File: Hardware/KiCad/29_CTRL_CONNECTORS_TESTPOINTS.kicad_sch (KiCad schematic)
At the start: 0 parts

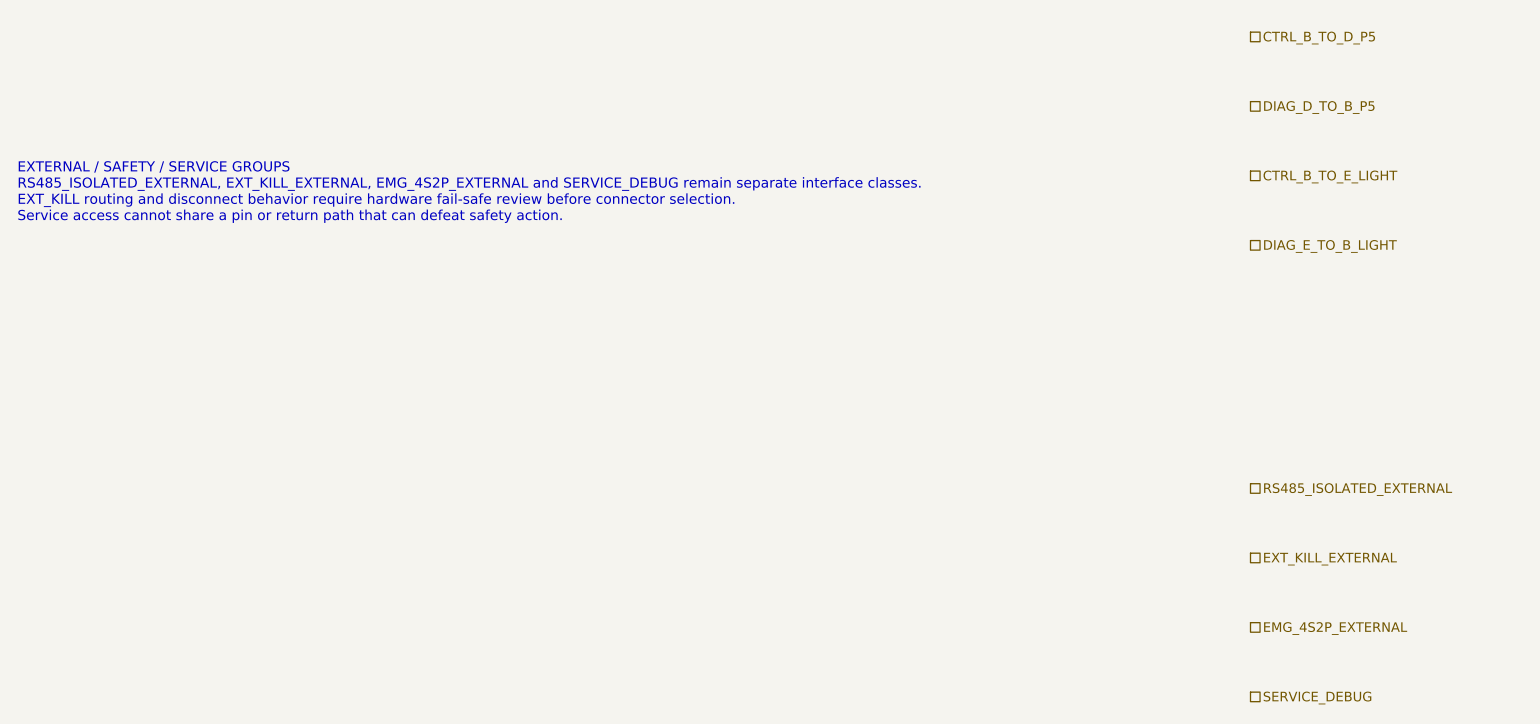
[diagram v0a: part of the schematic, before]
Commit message: hardware: align PCB-B external connector group names
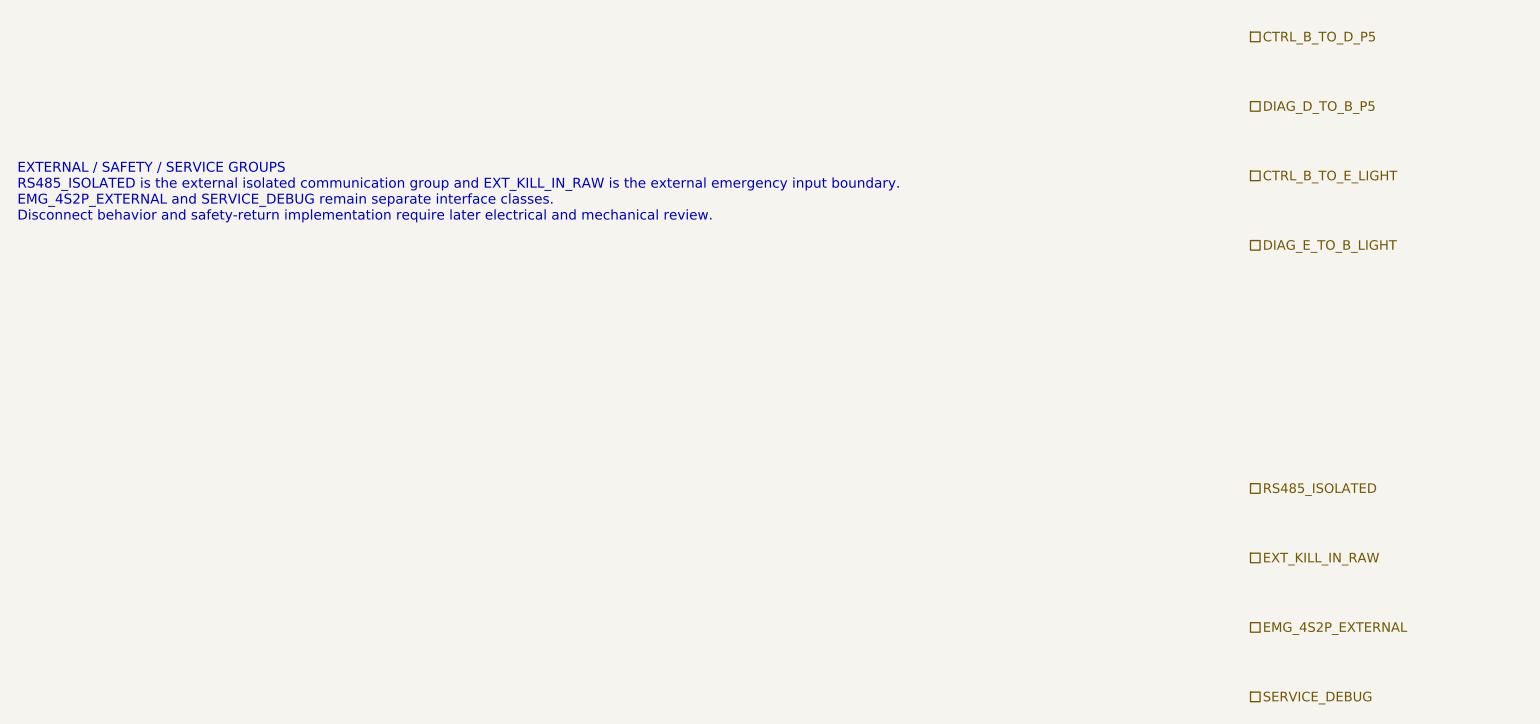
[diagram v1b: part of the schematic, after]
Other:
- note added: "EXTERNAL / SAFETY / SERVICE GROUPS RS485_ISOLATED is the external isolated communication group and EXT_KILL_IN_RAW is the external emergency input boundary. EMG_4S2P_EXTERNAL and SERVICE_DEBUG remain separate interface classes. Disconnect behavior and safety-return implementation require later electrical and mechanical review."
- note removed: "EXTERNAL / SAFETY / SERVICE GROUPS RS485_ISOLATED_EXTERNAL, EXT_KILL_EXTERNAL, EMG_4S2P_EXTERNAL and SERVICE_DEBUG remain separate interface classes. EXT_KILL routing and disconnect behavior require hardware fail-safe review before connector selection. Service access cannot share a pin or return path that can defeat safety action."
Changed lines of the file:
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@@
 		(title "29_CTRL_CONNECTORS_TESTPOINTS - logical connector and test boundary")
 		(date "2026-07-15")
-		(rev "B0")
+		(rev "B1")
 		(company "Gonoboben/plataVM")
-		(comment 1 "Architecture Level A/B: interboard, external, EMG and service interface grouping")
+		(comment 1 "Interface consistency: canonical RS485_ISOLATED and EXT_KILL_IN_RAW groups")
 		(comment 2 "No connector family, pin count, pinout, cable, testpoint technology or footprint selected")
 	)
@@
 		(uuid "ctrl-reserve-00000029-0000-4000-8000-000000000102")
 	)
-	(text "EXTERNAL / SAFETY / SERVICE GROUPS\nRS485_ISOLATED_EXTERNAL, EXT_KILL_EXTERNAL, EMG_4S2P_EXTERNAL and SERVICE_DEBUG remain separate interface classes.\nEXT_KILL routing and disconnect behavior require hardware fail-safe review before connector selection.\nService access cannot share a pin or return path that can defeat safety action."
+	(text "EXTERNAL / SAFETY / SERVICE GROUPS\nRS485_ISOLATED is the external isolated communication group and EXT_KILL_IN_RAW is the external emergency input boundary.\nEMG_4S2P_EXTERNAL and SERVICE_DEBUG remain separate interface classes.\nDisconnect behavior and safety-return implementation require later electrical and mechanical review."
 		(exclude_from_sim no)
 		(at 12 138 0)
-		(effects (font (size 1.16 1.16)) (justify left))
+		(effects (font (size 1.14 1.14)) (justify left))
 		(uuid "ctrl-reserve-00000029-0000-4000-8000-000000000103")
 	)
@@
 	(hierarchical_label "CTRL_B_TO_E_LIGHT" (shape passive) (exclude_from_sim no) (at 154 136 0) (effects (font (size 1.1 1.1)) (justify left)) (uuid "ctrl-reserve-00000029-0000-4000-8000-000000000208"))
 	(hierarchical_label "DIAG_E_TO_B_LIGHT" (shape passive) (exclude_from_sim no) (at 154 144 0) (effects (font (size 1.1 1.1)) (justify left)) (uuid "ctrl-reserve-00000029-0000-4000-8000-000000000209"))
-	(hierarchical_label "RS485_ISOLATED_EXTERNAL" (shape passive) (exclude_from_sim no) (at 154 172 0) (effects (font (size 1.1 1.1)) (justify left)) (uuid "ctrl-reserve-00000029-0000-4000-8000-000000000210"))
-	(hierarchical_label "EXT_KILL_EXTERNAL" (shape passive) (exclude_from_sim no) (at 154 180 0) (effects (font (size 1.1 1.1)) (justify left)) (uuid "ctrl-reserve-00000029-0000-4000-8000-000000000211"))
+	(hierarchical_label "RS485_ISOLATED" (shape passive) (exclude_from_sim no) (at 154 172 0) (effects (font (size 1.1 1.1)) (justify left)) (uuid "ctrl-reserve-00000029-0000-4000-8000-000000000210"))
+	(hierarchical_label "EXT_KILL_IN_RAW" (shape passive) (exclude_from_sim no) (at 154 180 0) (effects (font (size 1.1 1.1)) (justify left)) (uuid "ctrl-reserve-00000029-0000-4000-8000-000000000211"))
 	(hierarchical_label "EMG_4S2P_EXTERNAL" (shape passive) (exclude_from_sim no) (at 154 188 0) (effects (font (size 1.1 1.1)) (justify left)) (uuid "ctrl-reserve-00000029-0000-4000-8000-000000000212"))
 	(hierarchical_label "SERVICE_DEBUG" (shape passive) (exclude_from_sim no) (at 154 196 0) (effects (font (size 1.1 1.1)) (justify left)) (uuid "ctrl-reserve-00000029-0000-4000-8000-000000000213"))

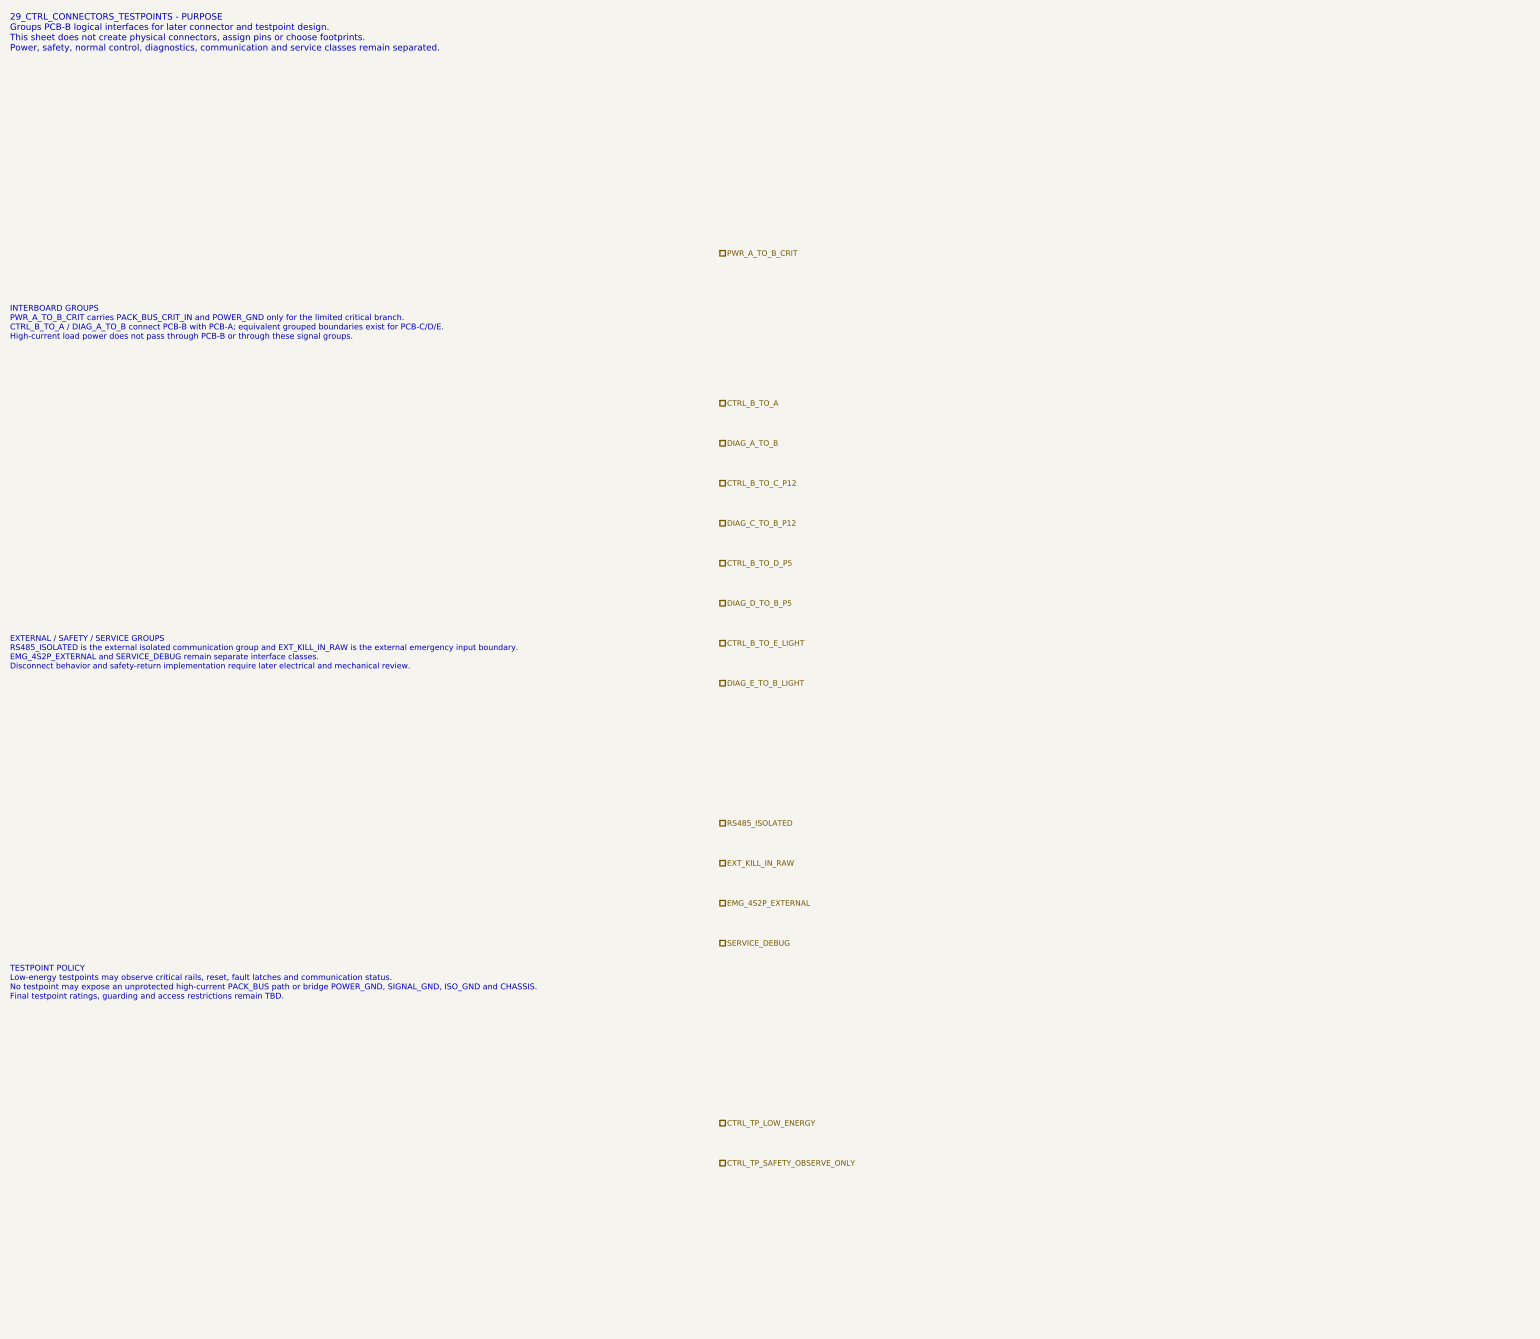
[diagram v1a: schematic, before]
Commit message: hardware: add CAN-FD and controlled ground net-tie connector boundaries
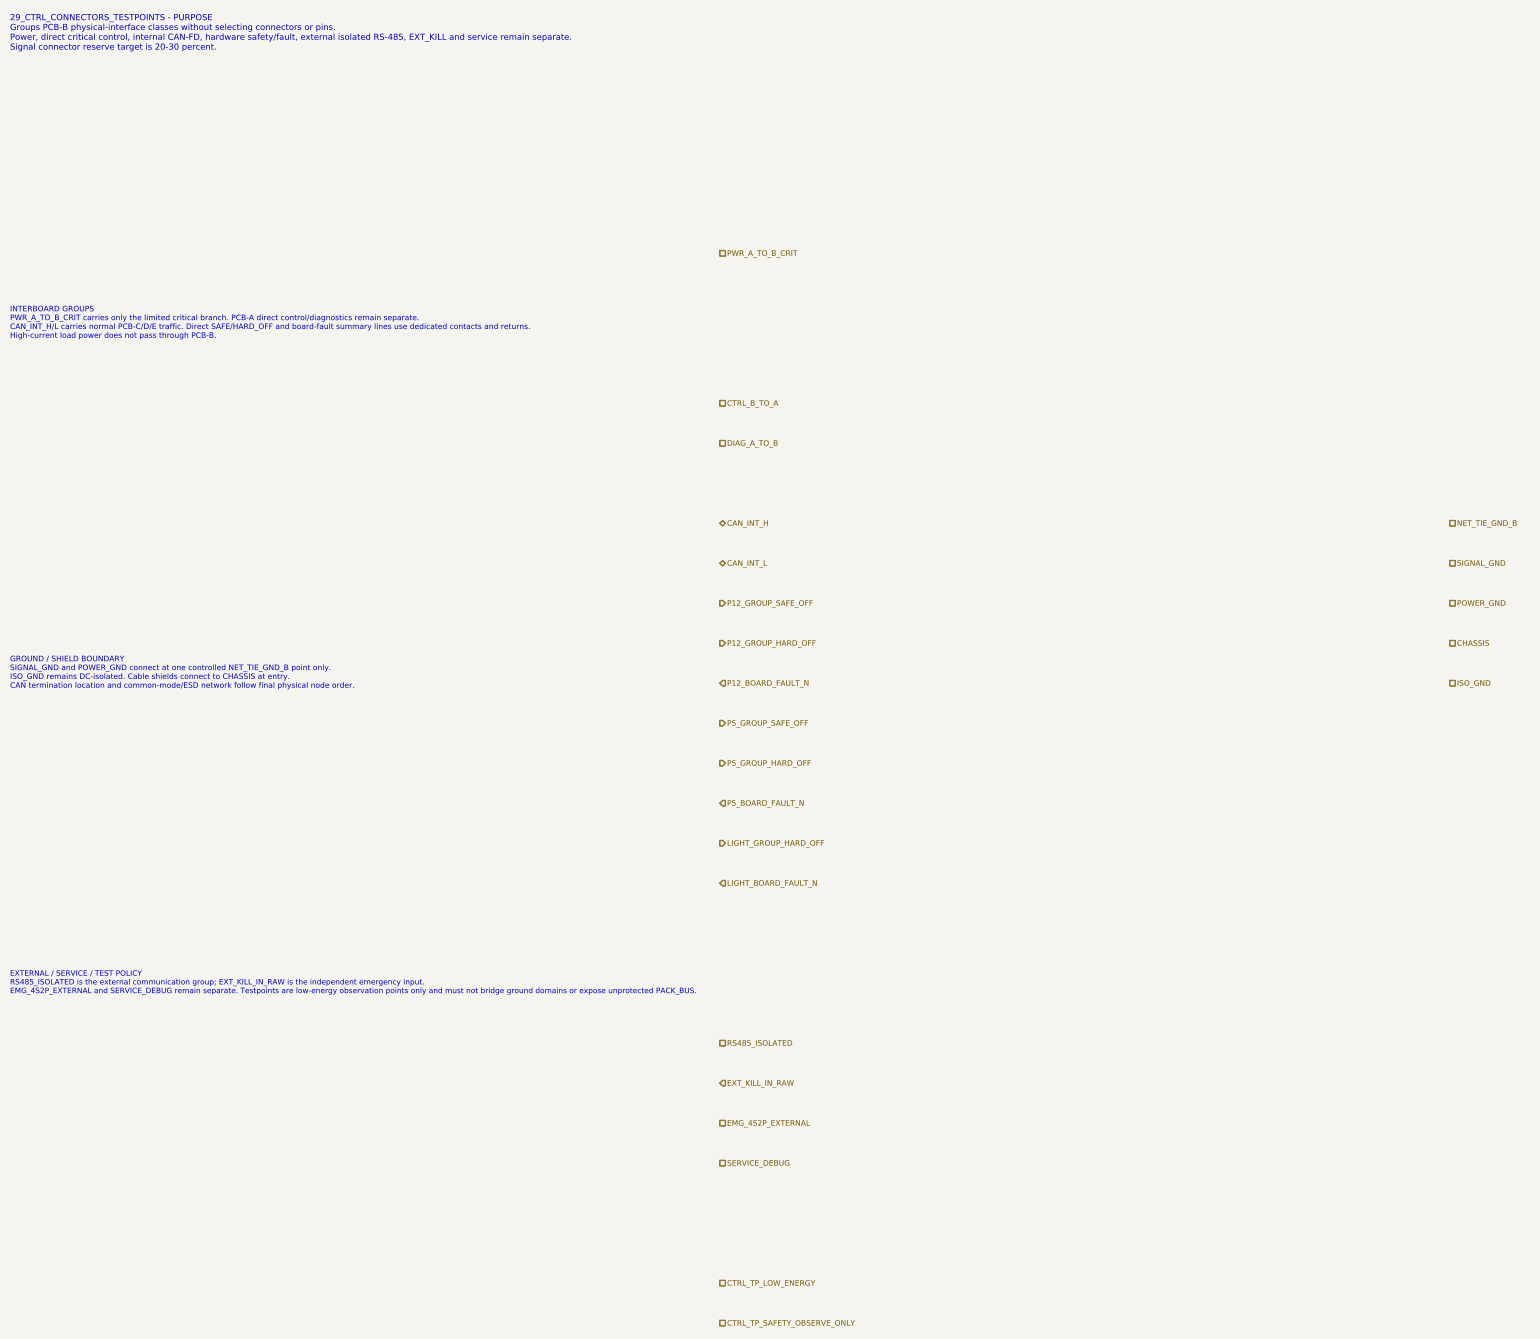
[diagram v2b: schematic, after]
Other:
- note added: "29_CTRL_CONNECTORS_TESTPOINTS - PURPOSE Groups PCB-B physical-interface classes without selecting connectors or pins. Power, direct critical control, internal CAN-FD, hardware safety/fault, external isolated RS-485, EXT_KILL and service remain separate. Signal connector reserve target is 20-30 percent."
- note added: "EXTERNAL / SERVICE / TEST POLICY RS485_ISOLATED is the external communication group; EXT_KILL_IN_RAW is the independent emergency input. EMG_4S2P_EXTERNAL and SERVICE_DEBUG remain separate. Testpoints are low-energy observation points only and must not bridge ground domains or expose unprotected PACK_BUS."
- note added: "GROUND / SHIELD BOUNDARY SIGNAL_GND and POWER_GND connect at one controlled NET_TIE_GND_B point only. ISO_GND remains DC-isolated. Cable shields connect to CHASSIS at entry. CAN termination location and common-mode/ESD network follow final physical node order."
- note added: "INTERBOARD GROUPS PWR_A_TO_B_CRIT carries only the limited critical branch. PCB-A direct control/diagnostics remain separate. CAN_INT_H/L carries normal PCB-C/D/E traffic. Direct SAFE/HARD_OFF and board-fault summary lines use dedicated contacts and returns. High-current load power does not pass through PCB-B."
- note removed: "29_CTRL_CONNECTORS_TESTPOINTS - PURPOSE Groups PCB-B logical interfaces for later connector and testpoint design. This sheet does not create physical connectors, assign pins or choose footprints. Power, safety, normal control, diagnostics, communication and service classes remain separated."
- note removed: "EXTERNAL / SAFETY / SERVICE GROUPS RS485_ISOLATED is the external isolated communication group and EXT_KILL_IN_RAW is the external emergency input boundary. EMG_4S2P_EXTERNAL and SERVICE_DEBUG remain separate interface classes. Disconnect behavior and safety-return implementation require later electrical and mechanical review."
- note removed: "INTERBOARD GROUPS PWR_A_TO_B_CRIT carries PACK_BUS_CRIT_IN and POWER_GND only for the limited critical branch. CTRL_B_TO_A / DIAG_A_TO_B connect PCB-B with PCB-A; equivalent grouped boundaries exist for PCB-C/D/E. High-current load power does not pass through PCB-B or through these signal groups."
- note removed: "TESTPOINT POLICY Low-energy testpoints may observe critical rails, reset, fault latches and communication status. No testpoint may expose an unprotected high-current PACK_BUS path or bridge POWER_GND, SIGNAL_GND, ISO_GND and CHASSIS. Final testpoint ratings, guarding and access restrictions remain TBD."
- title: 29_CTRL_CONNECTORS_TESTPOINTS - logical connector and test boundary -> 29_CTRL_CONNECTORS_TESTPOINTS - connector, CAN-FD and ground boundary
